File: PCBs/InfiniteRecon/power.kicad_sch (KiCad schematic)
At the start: 16 parts, among them J1 USB_C_Receptacle, Q1 AO3401A, U1 MCP73831-2-OT

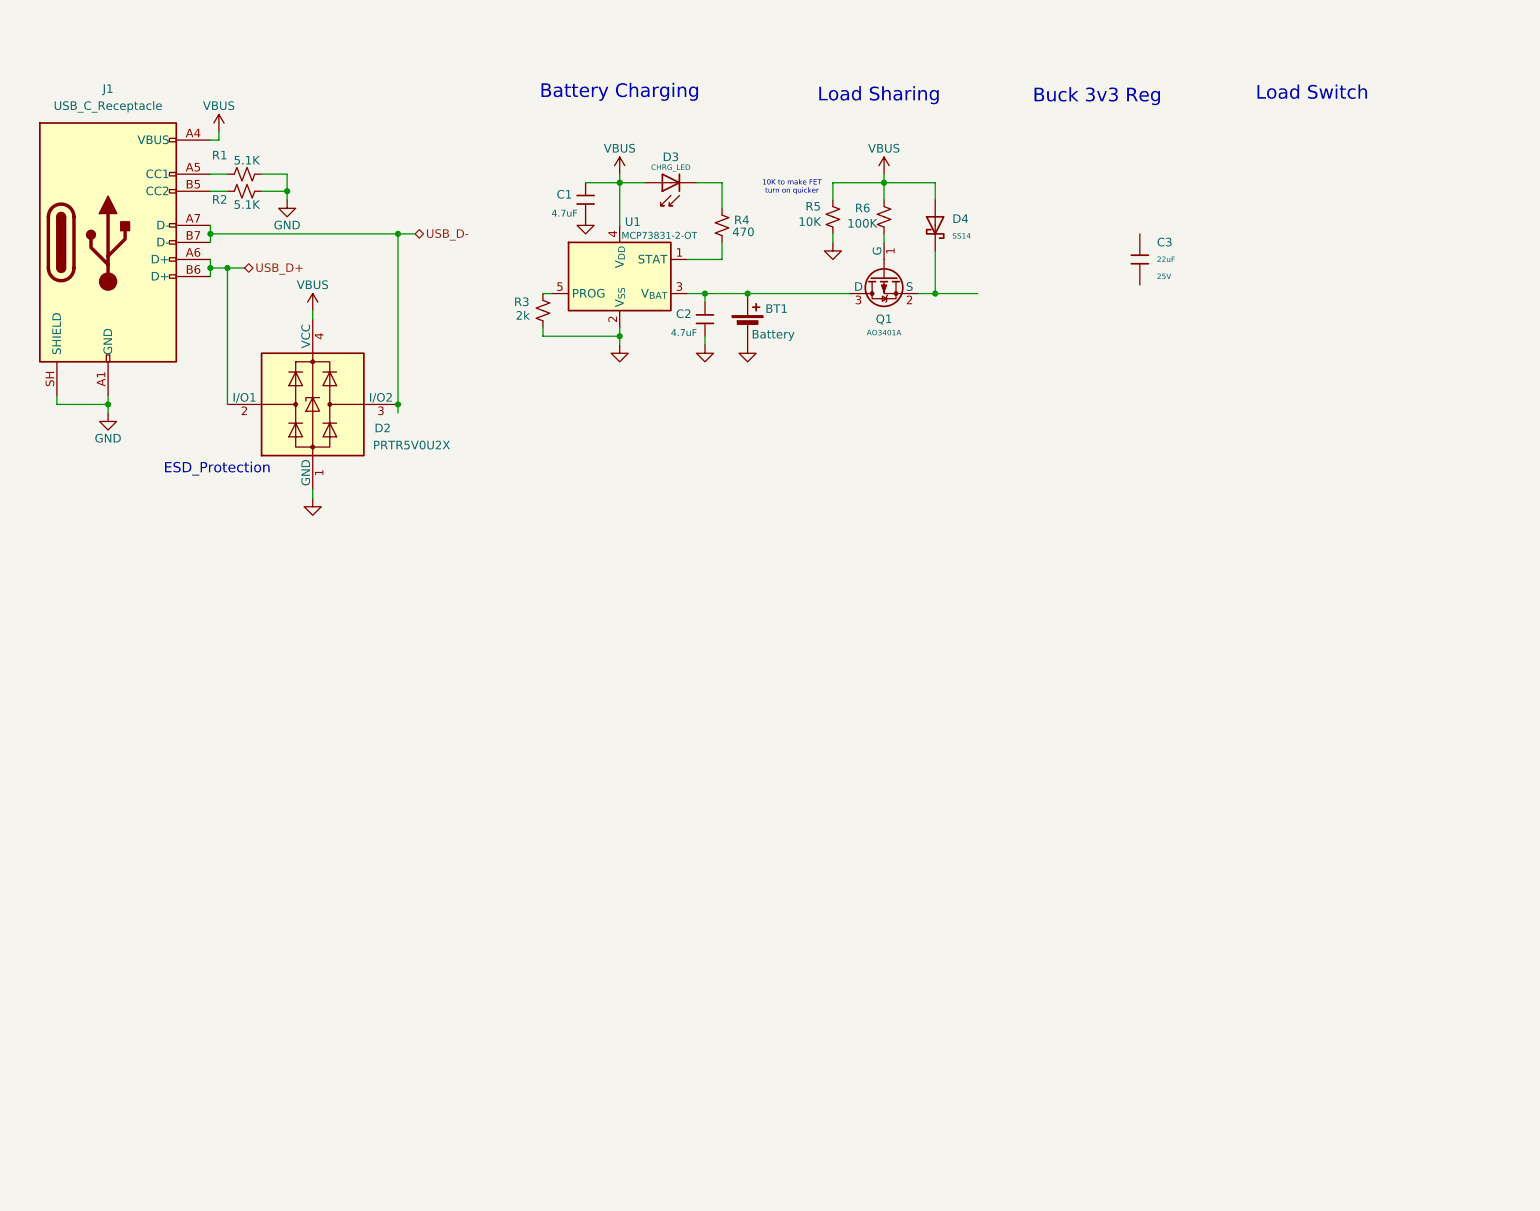
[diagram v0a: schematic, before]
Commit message: Finished Scem for the most part, awake me needs to look it over one more time
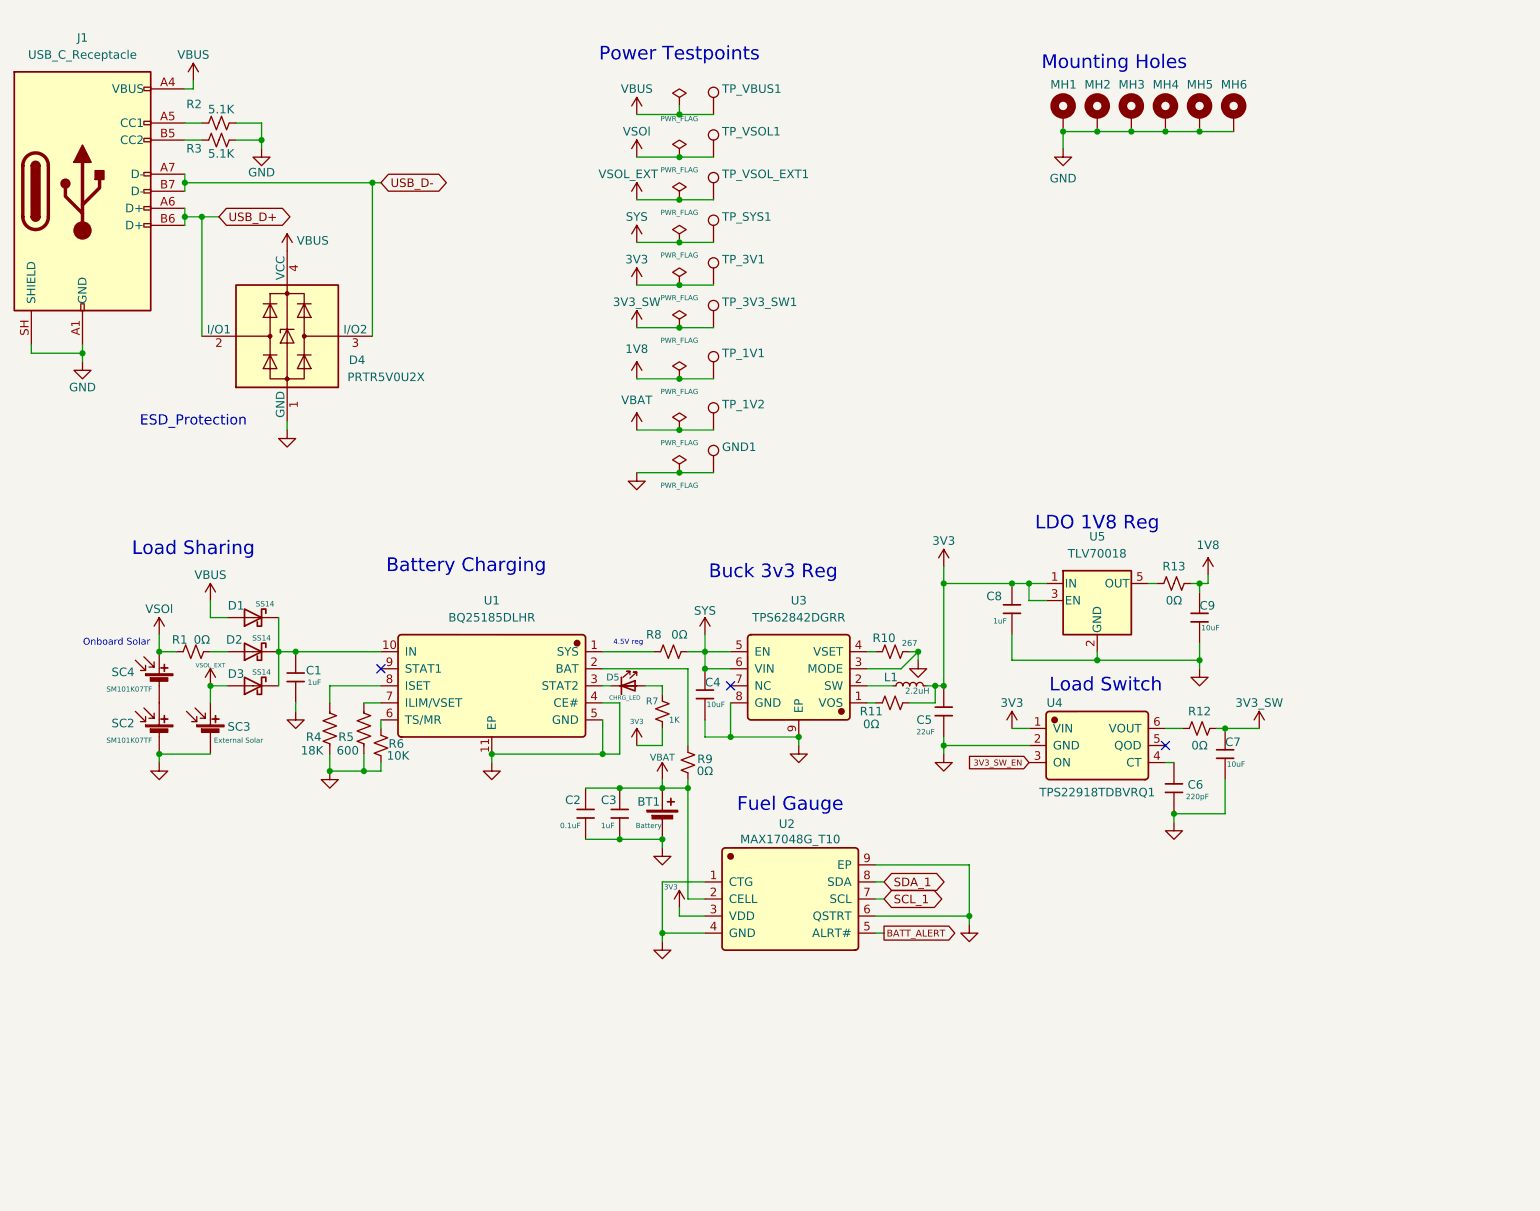
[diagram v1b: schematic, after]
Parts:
- removed C1, C2: 4.7uF, PCM_JLCPCB:C_0603, symbol PCM_JLCPCB-Capacitors:0603,4.7uF
- removed C3: 22uF, PCM_JLCPCB:C_0805, symbol PCM_JLCPCB-Capacitors:0805,22uF
- removed D3: CHRG_LED, PCM_JLCPCB:D_0805, symbol PCM_JLCPCB-Diodes:LED,0805,Green
- removed D4: SS14, PCM_JLCPCB:D_SMA, symbol PCM_JLCPCB-Diodes:Schottky,SS14
- removed Q1: AO3401A, PCM_JLCPCB:Q_SOT-23, symbol PCM_JLCPCB-Transistors:PMOS,AO3401A
- removed R3: 2k, Resistor_SMD:R_0402_1005Metric, symbol Device:R_Small_US
- removed R4: 470, Resistor_SMD:R_0402_1005Metric, symbol Device:R_Small_US
- removed R5: 10K, Resistor_SMD:R_0402_1005Metric, symbol Device:R_Small_US
- removed U1: MCP73831-2-OT, Package_TO_SOT_SMD:SOT-23-5, symbol Battery_Management:MCP73831-2-OT
- added C1, C3, C8: 1uF, PCM_JLCPCB:C_0603, symbol PCM_JLCPCB-Capacitors:0603,1uF
- added C2: 0.1uF, PCM_JLCPCB:C_0402, symbol PCM_JLCPCB-Capacitors:0402,100nF
- added C4, C7, C9: 10uF, PCM_JLCPCB:C_0603, symbol PCM_JLCPCB-Capacitors:0603,10uF
- added C5: 22uF, PCM_JLCPCB:C_0805, symbol PCM_JLCPCB-Capacitors:0805,22uF
- added C6: 220pF, PCM_JLCPCB:C_0402, symbol PCM_JLCPCB-Capacitors:0402,220pF
- added D1, D2, D3: SS14, PCM_JLCPCB:D_SMA, symbol PCM_JLCPCB-Diodes:Schottky,SS14
- added D5: CHRG_LED, PCM_JLCPCB:D_0805, symbol PCM_JLCPCB-Diodes:LED,0805,Green
- added GND1, TP_1V1, TP_1V2, TP_3V3_SW1: TestPoint, symbol Connector:TestPoint
- added L1: 2.2uH, PCM_JLCPCB:OSC-SMD_L5.0-W3.2, symbol Device:L_Small
- added MH1, MH2, MH3, MH4, MH5, MH6: MountingHole_Pad, MountingHole:MountingHole_2.2mm_M2_DIN965_Pad, symbol Mechanical:MountingHole_Pad
- added R1, R11, R12, R13, R8, R9: 0Ω, Resistor_SMD:R_0603_1608Metric_Pad0.98x0.95mm_HandSolder, symbol Device:R_Small_US
- added R10: 267, Resistor_SMD:R_0603_1608Metric, symbol Device:R_Small_US
- added R4: 18K, Resistor_SMD:R_01005_0402Metric, symbol Device:R_US
- added R5: 600, Resistor_SMD:R_01005_0402Metric, symbol Device:R_US
- added R7: 1K, PCM_JLCPCB:R_0402, symbol Device:R_Small_US
- added SC2, SC4: SM101K07TF, ssi_solarcell:SM101K07TF, symbol ssi_solarcell:SM101K07TF
- added SC3: External Solar, Connector_JST:JST_PH_S2B-PH-SM4-TB_1x02-1MP_P2.00mm_Horizontal, symbol Device:Solar_Cell
- added TP_3V1, TP_SYS1, TP_VBUS1, TP_VSOL1, TP_VSOL_EXT1: TestPoint, TestPoint:TestPoint_Pad_1.5x1.5mm, symbol Connector:TestPoint
- added U1: BQ25185DLHR, Package_DFN_QFN:Texas_DLH0010A_WSON-10-1EP_2.2x2mm_P0.4mm_EP0.9x1.5mm, symbol JLCImport:BQ25185DLHR
- added U2: MAX17048G_T10, Package_DFN_QFN:TDFN-8-1EP_3x2mm_P0.5mm_EP1.3x1.4mm, symbol JLCImport:MAX17048G_T10
- added U3: TPS62842DGRR, PCM_JLCPCB:ESOP-8_L4.9-W3.9-P1.27-LS6.0-BL-EP, symbol JLCImport:TPS62842DGRR
- added U4: TPS22918TDBVRQ1, Package_TO_SOT_SMD:SOT-23-6, symbol JLCImport:TPS22918TDBVRQ1
- added U5: TLV70018, Package_TO_SOT_SMD:SOT-23-5, symbol Regulator_Linear:TLV70018_SOT23-5
- BT1: footprint Connector_JST:JST_PH_S2B-PH-K_1x02_P2.00mm_Horizontal -> Connector_JST:JST_PH_S2B-PH-SM4-TB_1x02-1MP_P2.00mm_Horizontal
- R6: value 100K -> 10K; footprint Resistor_SMD:R_0402_1005Metric -> Resistor_SMD:R_01005_0402Metric
- renumbered D2 to D4, R1 to R2, R2 to R3
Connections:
- net GND: now also R6.2, C1.2, C2.2, C3.2, C4.2, C5.2, C6.2, C7.2, C8.2, C9.2, GND1.1, MH1.1, MH2.1, MH3.1, MH4.1, MH5.1, MH6.1, R10.2, R4.2, R5.2, SC2.2 (-), SC3.2 (-), U1.11 (EP), U1.4 (CE#), U1.5 (GND), U2.1 (CTG), U2.4 (GND), U2.6 (QSTRT), U2.9 (EP), U3.3 (MODE), U3.8 (GND), U3.9 (EP), U4.2 (GND), U5.2 (GND)
- net VBUS: now also D1.2, TP_VBUS1.1; no longer R6.2
- net VBAT: now reaches BT1.1 (+)
- net VBAT: now also C2.1, C3.1, R9.1, TP_1V2.1, U2.2 (CELL)
- net at R6.1: now also U1.6 (TS/MR)
- new net: R4.1, U1.8 (ISET)
- new net: C1.1, D1.1, D2.1, D3.1, U1.10 (IN)
- new net: R5.1, U1.7 (ILIM/VSET)
- new net: C6.1, U4.4 (CT)
- new net: D5.1, U1.3 (STAT2)
- new net: D5.2, R7.2
- new net: SC2.1 (+), SC4.2 (-)
- new net: R12.2, U4.6 (VOUT)
- new net: D2.2, R1.2
- new net: R8.1, U1.1 (SYS)
- new net: R9.2, U1.2 (BAT)
- new net: R13.2, U5.5 (OUT)
- new net: R10.1, U3.4 (VSET)
- new net: R11.1, U3.1 (VOS)
- new net: L1.1, U3.2 (SW)
- new net 1V8: C9.1, R13.1, TP_1V1.1
- new net 3V3: C5.1, C8.1, L1.2, R11.2, R7.1, TP_3V1.1, U2.3 (VDD), U4.1 (VIN), U5.1 (IN), U5.3 (EN)
- new net 3V3_SW: C7.1, R12.1, TP_3V3_SW1.1
- new net 3V3_SW_EN: U4.3 (ON)
- new net BATT_ALERT: U2.5 (ALRT#)
- new net SCL_1: U2.7 (SCL)
- new net SDA_1: U2.8 (SDA)
- new net SYS: C4.1, R8.2, TP_SYS1.1, U3.5 (EN), U3.6 (VIN)
- new net VSOL_EXT: D3.2, SC3.1 (+), TP_VSOL_EXT1.1
- new net VSOl: R1.1, SC4.1 (+), TP_VSOL1.1
- no-connect marks 0 -> 3
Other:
- note added: "4.5V reg"
- note added: "Fuel Gauge"
- note added: "LDO 1V8 Reg"
- note added: "Mounting Holes"
- note added: "Onboard Solar"
- note added: "Power Testpoints"
- note removed: "10K to make FET turn on quicker"
- moved on the sheet: D4, J1, R2, R3

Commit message: Fixed footprints and some not connected caps
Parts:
- R4, R5, R6: footprint Resistor_SMD:R_01005_0402Metric -> Resistor_SMD:R_0402_1005Metric
- R7: footprint PCM_JLCPCB:R_0402 -> Resistor_SMD:R_0402_1005Metric
- renumbered C8 to C6, C6 to C7, C9 to C8, C7 to C9, R13 to R12, R12 to R13, SC4 to SC1, U5 to U4, U4 to U5

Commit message: Finished scem
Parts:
- added C38, C41: 1uF, PCM_JLCPCB:C_0603, symbol PCM_JLCPCB-Capacitors:0603,1uF
- added C39: 10uF, PCM_JLCPCB:C_0603, symbol PCM_JLCPCB-Capacitors:0603,10uF
- added C40, C42, C43: 0.1uF, PCM_JLCPCB:C_0402, symbol PCM_JLCPCB-Capacitors:0402,100nF
- added R36: 0Ω, Resistor_SMD:R_0603_1608Metric_Pad0.98x0.95mm_HandSolder, symbol Device:R_Small_US
- added R37: 100K, PCM_JLCPCB:R_0402, symbol Device:R_Small_US
- added TP_1V3: TestPoint, TestPoint:TestPoint_Pad_1.5x1.5mm, symbol Connector:TestPoint
- added U11: TLV70018, Package_TO_SOT_SMD:SOT-23-5, symbol Regulator_Linear:TLV70018_SOT23-5
- GND1, TP_3V3_SW1: footprint (none) -> TestPoint:TestPoint_Pad_1.5x1.5mm
- R4: value 18K -> 600
- R5: value 600 -> 18k
- TP_1V8: renamed from TP_1V1; footprint (none) -> TestPoint:TestPoint_Pad_1.5x1.5mm
- TP_1V8_SW1: renamed from TP_1V2; footprint (none) -> TestPoint:TestPoint_Pad_1.5x1.5mm
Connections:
- net 3V3: now also C40.1, C41.1, C42.1, C43.1, R37.1
- net 3V3_SW: now also C38.1, U11.1 (IN), U11.3 (EN)
- net BATT_ALERT: now also R37.2
- net GND: now also C38.2, C39.2, C40.2, C41.2, C42.2, C43.2, U11.2 (GND)
- net VBAT: now also TP_1V3.1; no longer TP_1V8_SW1.1
- new net: R36.2, U11.5 (OUT)
- new net 1V8_SW: C39.1, R36.1, TP_1V8_SW1.1
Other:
- note added: "Decoupling"
- note added: "LDO 1V8_SW"
- note added: "Not for this entire page"
- moved on the sheet: GND1, TP_1V8, TP_1V8_SW1, TP_3V1, TP_3V3_SW1, TP_SYS1, TP_VBUS1, TP_VSOL1, TP_VSOL_EXT1

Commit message: Reanotated
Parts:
- renumbered C42 to C1, C6 to C10, C7 to C11, C8 to C12, C9 to C13, C38 to C14, C39 to C15, C43 to C2, C1 to C3, C2 to C4, C3 to C5, C40 to C6, C4 to C7, C5 to C8, C41 to C9, R37 to R12, R12 to R13, R13 to R14, R36 to R15, TP_1V8 to TP_1V1, TP_1V3 to TP_1V2, U11 to U6

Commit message: Added Mics
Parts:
- U2: footprint Package_DFN_QFN:TDFN-8-1EP_3x2mm_P0.5mm_EP1.3x1.4mm -> Package_DFN_QFN:DFN-8-1EP_2x2mm_P0.5mm_EP0.9x1.3mm
- U3: footprint PCM_JLCPCB:ESOP-8_L4.9-W3.9-P1.27-LS6.0-BL-EP -> Package_SO:HVSSOP-8-1EP_3x3mm_P0.65mm_EP1.57x1.89mm_ThermalVias
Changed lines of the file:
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@@
 		)
 		(property "Value" "PWR_FLAG"
-			(at 119.38 26.035 0)
+			(at 119.38 26.416 0)
 			(show_name no)
 			(do_not_autoplace no)
@@
 			)
 		)
-		(property "Footprint" "Package_DFN_QFN:TDFN-8-1EP_3x2mm_P0.5mm_EP1.3x1.4mm"
+		(property "Footprint" "Package_DFN_QFN:DFN-8-1EP_2x2mm_P0.5mm_EP0.9x1.3mm"
 			(at 135.89 146.05 0)
 			(hide yes)
@@
 			)
 		)
-		(property "Footprint" "PCM_JLCPCB:ESOP-8_L4.9-W3.9-P1.27-LS6.0-BL-EP"
+		(property "Footprint" "Package_SO:HVSSOP-8-1EP_3x3mm_P0.65mm_EP1.57x1.89mm_ThermalVias"
 			(at 137.16 113.03 0)
 			(hide yes)

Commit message: lots of routing to be done
maybe its time to descope...
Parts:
- removed GND1: TestPoint, TestPoint:TestPoint_Pad_1.5x1.5mm, symbol Connector:TestPoint
- removed MH4, MH5, MH6: MountingHole_Pad, MountingHole:MountingHole_2.2mm_M2_DIN965_Pad, symbol Mechanical:MountingHole_Pad
- J1: footprint Connector_USB:USB_C_Receptacle_G-Switch_GT-USB-7010ASV -> Connector_USB:USB_C_Receptacle_GCT_USB4110
- R12: footprint PCM_JLCPCB:R_0402 -> Resistor_SMD:R_0402_1005Metric

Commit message: More layout
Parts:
- added C44, C45: 0.1uF, PCM_JLCPCB:C_0402, symbol PCM_JLCPCB-Capacitors:0402,100nF
- J1: footprint Connector_USB:USB_C_Receptacle_GCT_USB4110 -> Connector_USB:USB_C_Receptacle_GCT_USB4105-xx-A_16P_TopMnt_Horizontal
- R4: value 600 -> 1K; LCSC (none) -> C11702
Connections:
- net 3V3: now also C45.1
- net GND: now also C44.2, C45.2
- net SYS: now also C44.1
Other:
- moved on the sheet: C6

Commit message: Layout more or less done. Still missing i2c pullups and need to redo pinout
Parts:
- removed C4: 0.1uF, PCM_JLCPCB:C_0402, symbol PCM_JLCPCB-Capacitors:0402,100nF
- removed R1: 0Ω, Resistor_SMD:R_0603_1608Metric_Pad0.98x0.95mm_HandSolder, symbol Device:R_Small_US
- removed TP_SYS1: TestPoint, TestPoint:TestPoint_Pad_1.5x1.5mm, symbol Connector:TestPoint
- renumbered C9 to C10, C10 to C11, C11 to C12, C12 to C13, C13 to C14, C14 to C15, C15 to C16, C45 to C3, C6 to C4, C44 to C5, C3 to C6, C5 to C7, C7 to C8, C8 to C9, R2 to R1, R11 to R10, R12 to R11, R13 to R12, R14 to R13, R15 to R14, R3 to R2, R4 to R3, R5 to R4, R6 to R5, R7 to R6, R8 to R7, R9 to R8, R10 to R9
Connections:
- net 3V3: no longer C2.1
- net 3V3_SW: now also C2.1
- net VSOl: now also D2.2
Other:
- moved on the sheet: C3, C4, SC1, SC2, SC3
